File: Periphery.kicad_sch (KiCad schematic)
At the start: 22 parts, among them SW1 Mitsumi R-667996, SW2 Mitsumi R-667996, U2 SN74LV595A, U3 THVD1420DRLR, U4 RS31340B, U5 SN74LV595A, U6 TS5A3159DCK

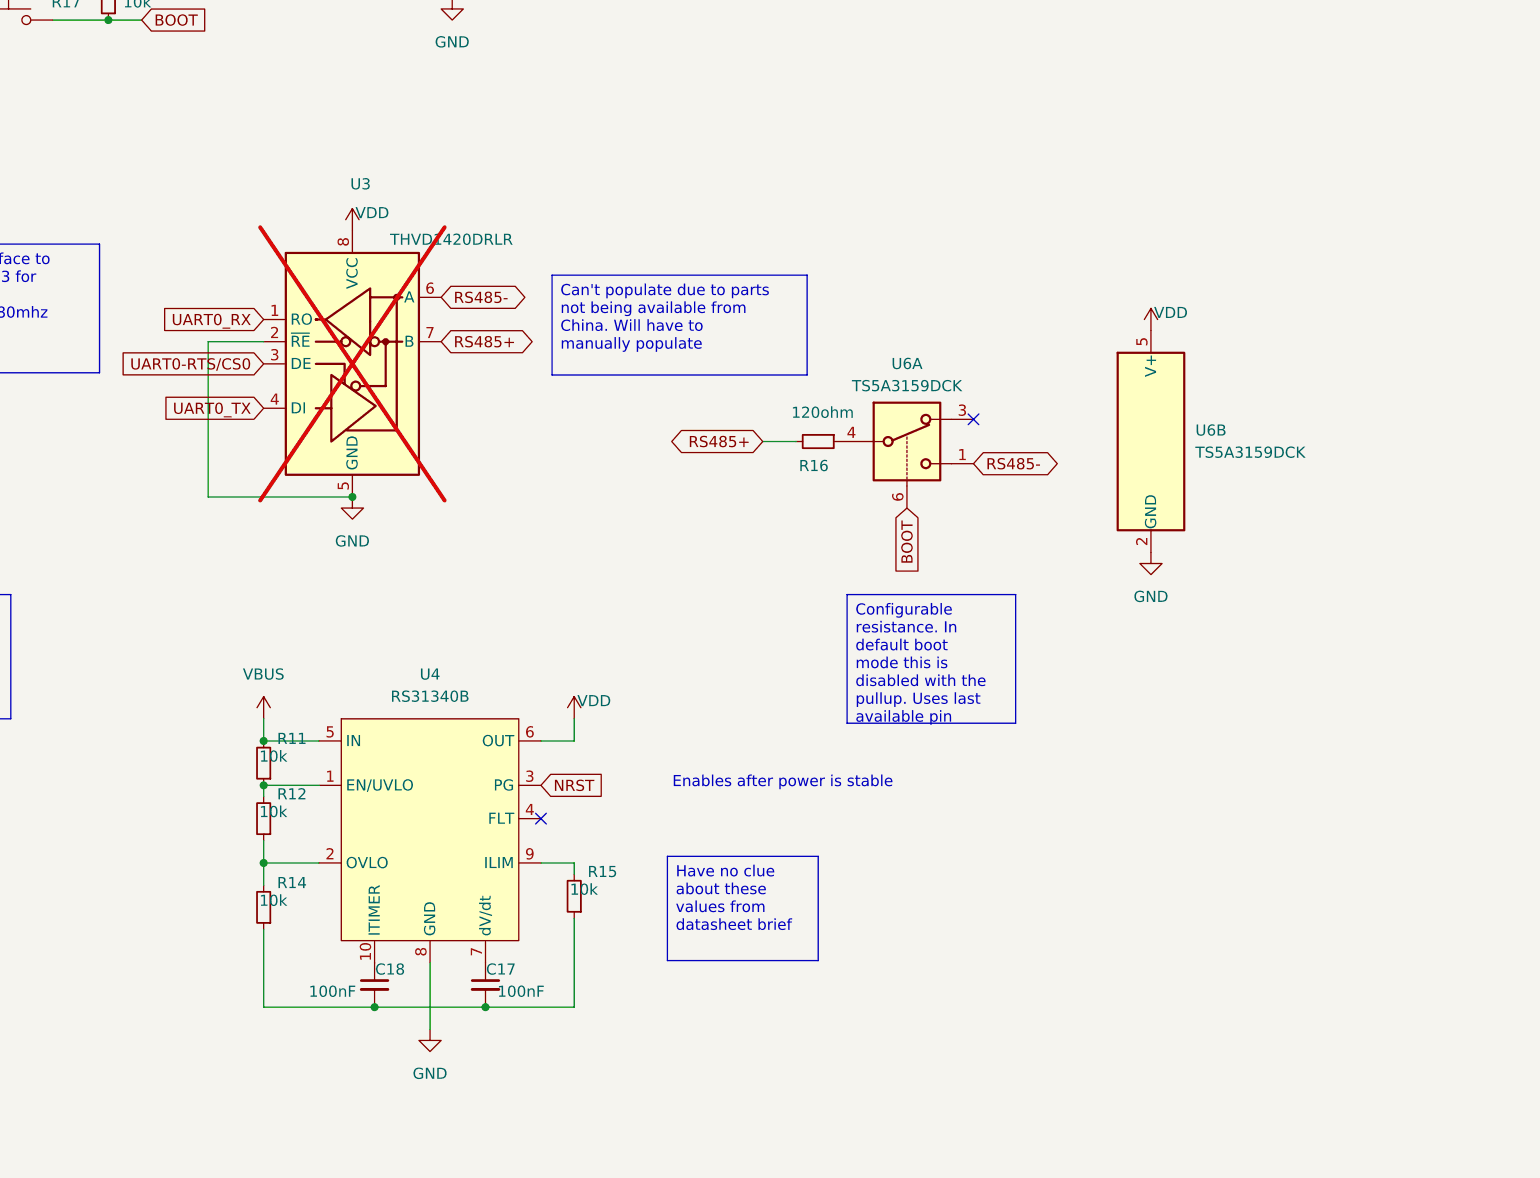
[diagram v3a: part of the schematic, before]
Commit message: Got proper values and replacement eFuse
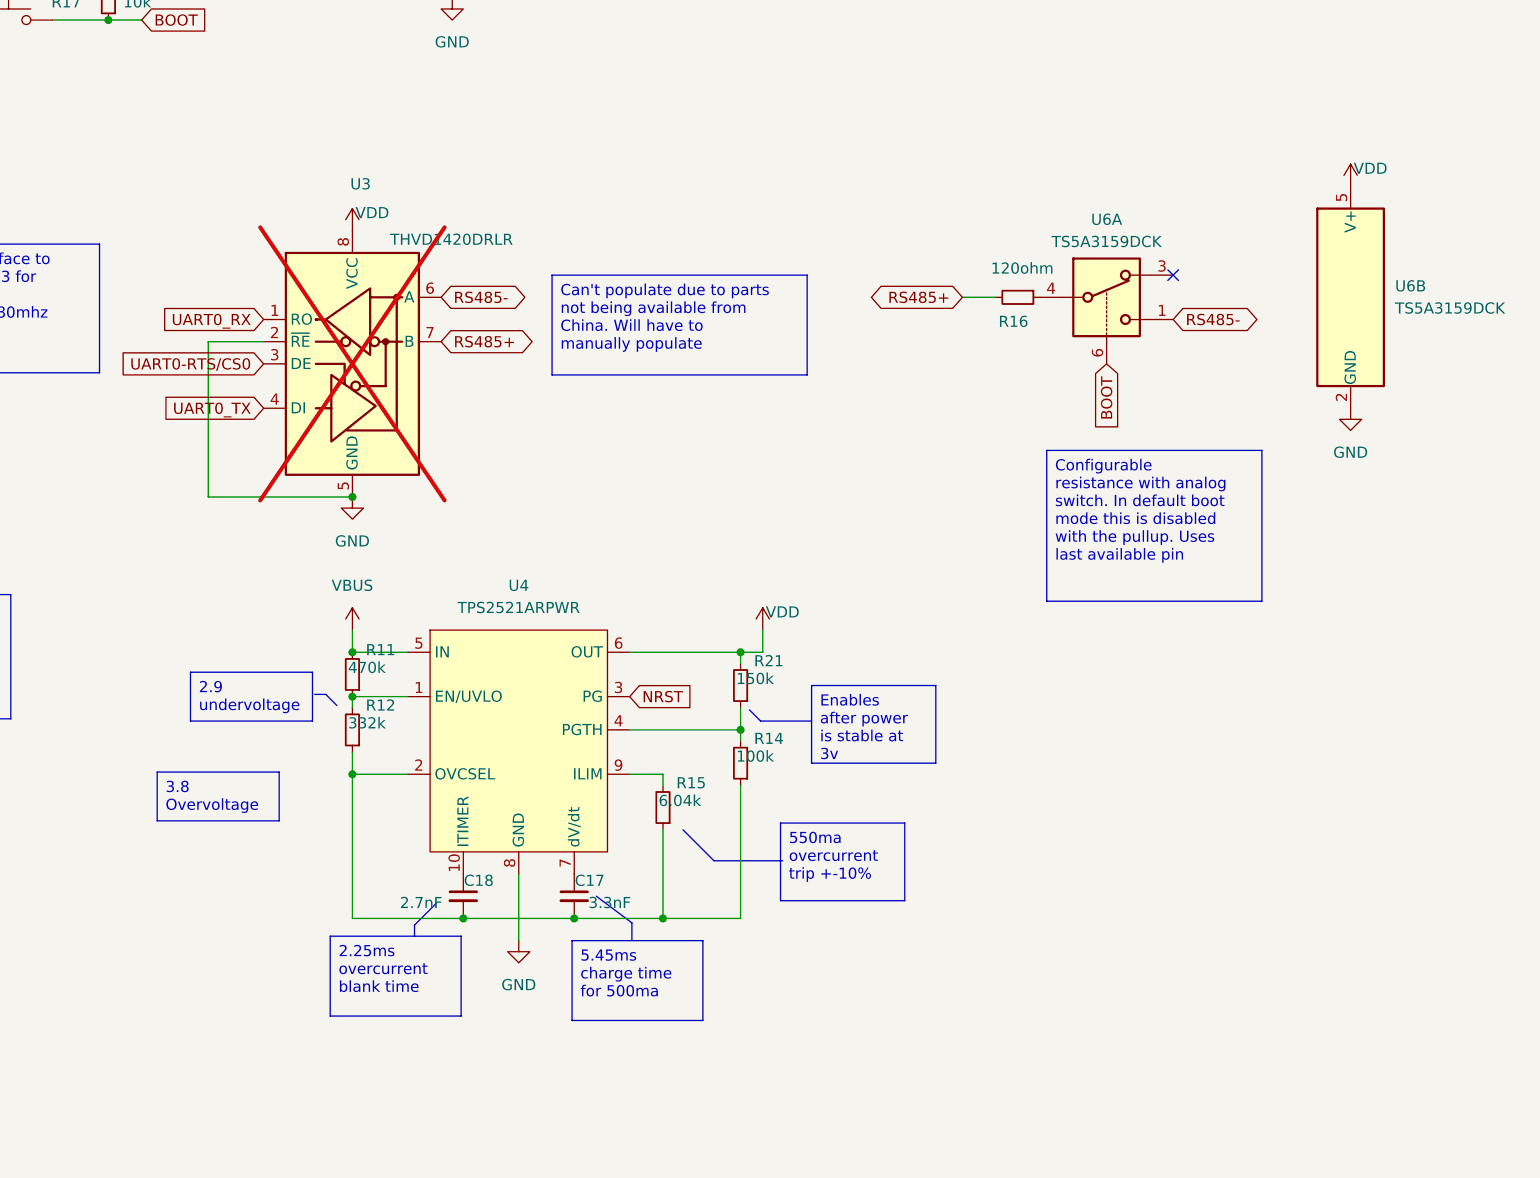
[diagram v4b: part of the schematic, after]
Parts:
- added R21: 150k, Resistor_SMD:R_0402_1005Metric, symbol Device:R_Small
- C17: value 100nF -> 3.3nF
- C18: value 100nF -> 2.7nF
- R11: value 10k -> 470k
- R12: value 10k -> 332k
- R14: value 10k -> 100k
- R15: value 10k -> 6.04k
- U4: value RS31340B -> TPS2521ARPWR; symbol custom_Power_Management:RS31340 -> custom_Power_Management:TPS2521xx
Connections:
- net VDD: now also R21.2
- net at C17.2, C18.2, R14.1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: now also R12.1, U4.2 (OVCSEL)
- net at U4.4 (PGTH): now also R14.2, R21.1
- no-connect marks 3 -> 2
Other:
- note removed: "Enables after power is stable"
- moved on the sheet: C17, C18, R11, R12, R15, R16, U4, U6A, U6B

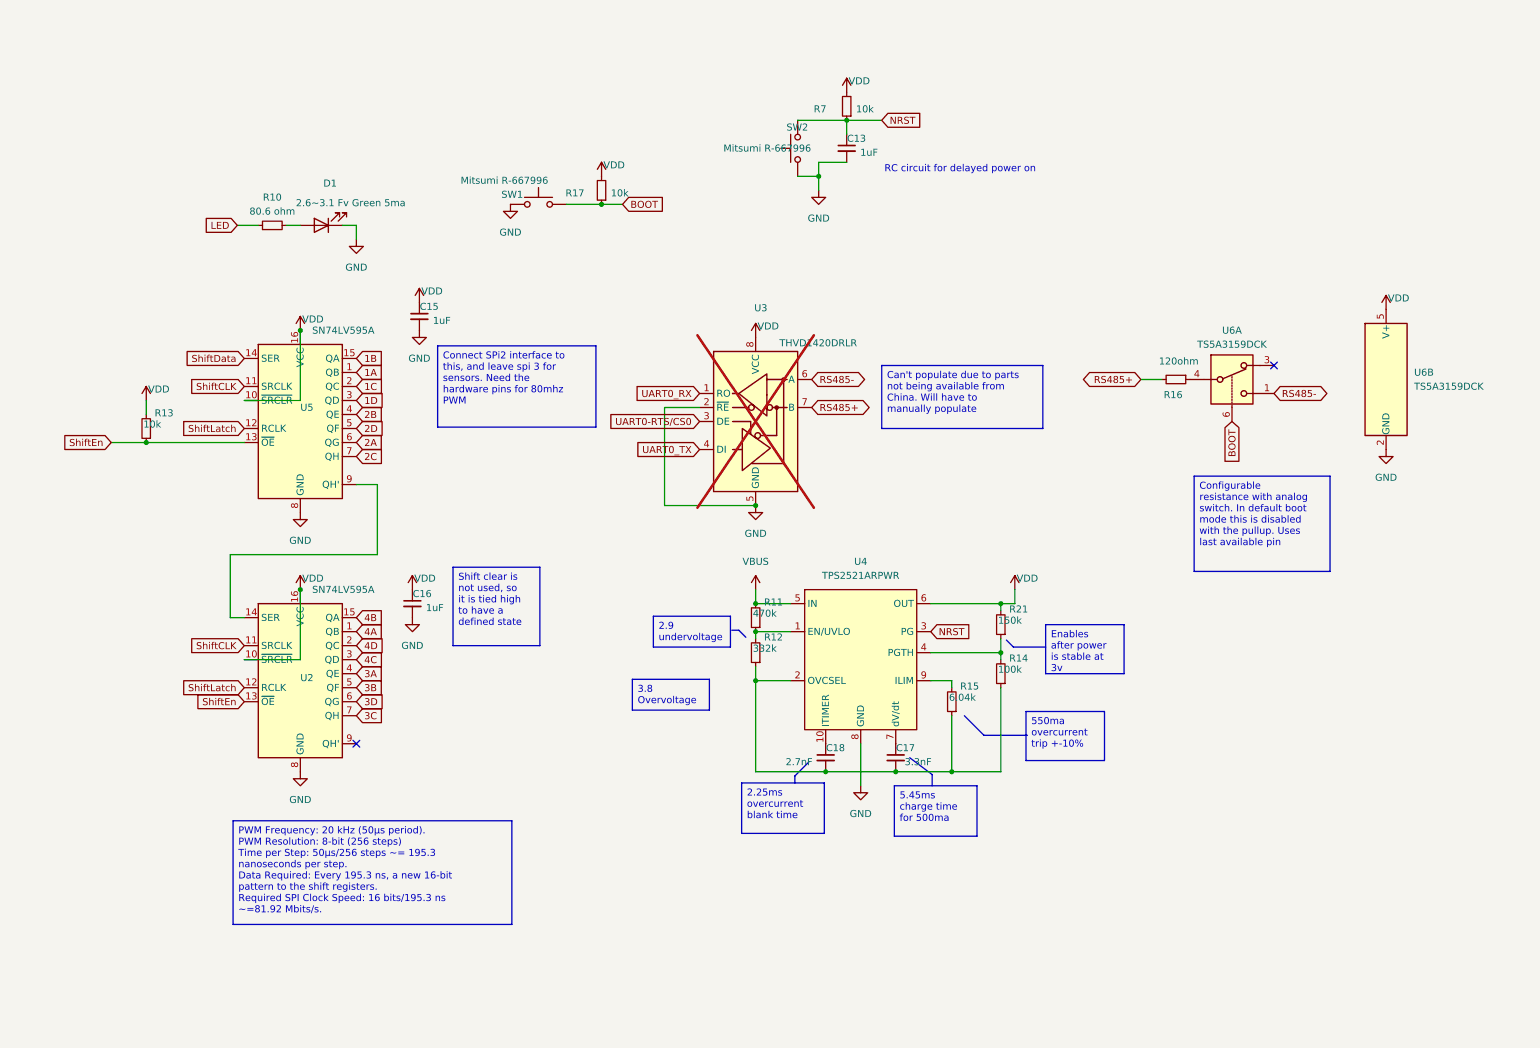
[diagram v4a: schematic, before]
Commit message: Reorganized and made schematic clearer
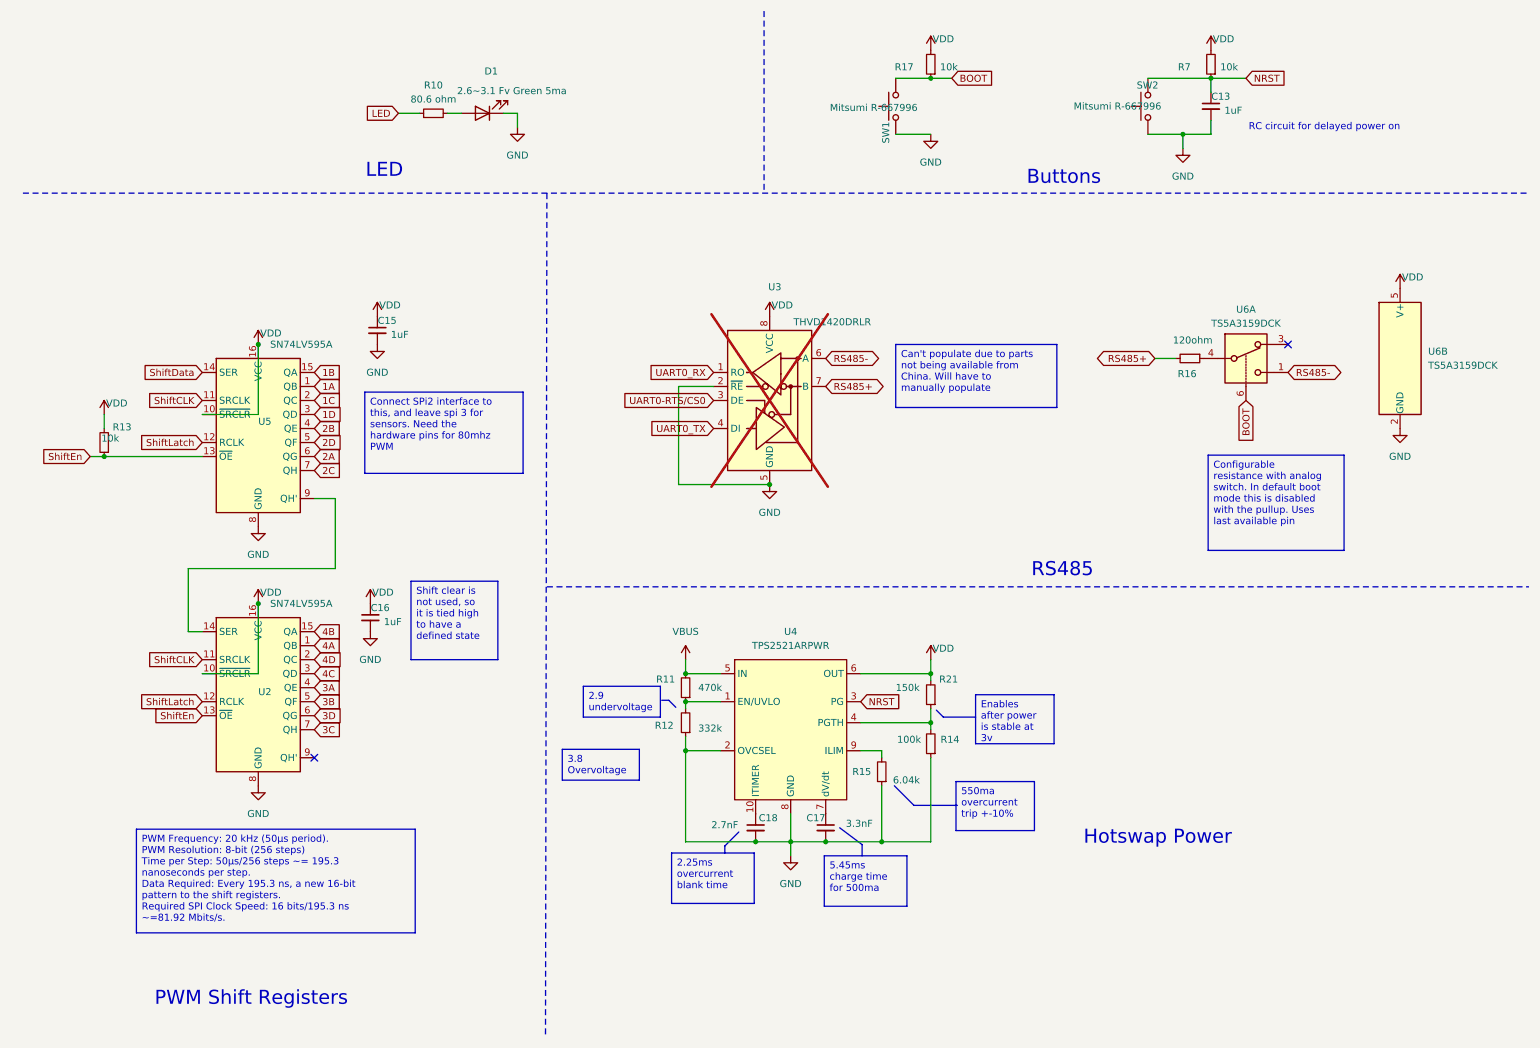
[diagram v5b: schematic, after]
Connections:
- net GND: now also C17.2, C18.2, R12.1, R14.1, R15.1, U2.17 (GND), U4.2 (OVCSEL), U5.17 (GND)
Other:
- note added: "Buttons"
- note added: "Hotswap Power"
- note added: "LED"
- note added: "PWM Shift Registers"
- note added: "RS485"
- moved on the sheet: C13, C15, C16, C17, C18, D1, R10, R11, R12, R13, R14, R15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

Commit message: Corrected footprint, started reconnect nets PCB
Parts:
- U4: footprint custom_Power_QFN:QFN-10-1EP_2x2mm_P0.5mm -> custom_Power_QFN:QFN-10_10VQFN_2x2mm_P0.5mm
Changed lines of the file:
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@@
 			)
 		)
-		(property "Footprint" "custom_Power_QFN:QFN-10-1EP_2x2mm_P0.5mm"
+		(property "Footprint" "custom_Power_QFN:QFN-10_10VQFN_2x2mm_P0.5mm"
 			(at 151.13 142.24 0)
 			(effects

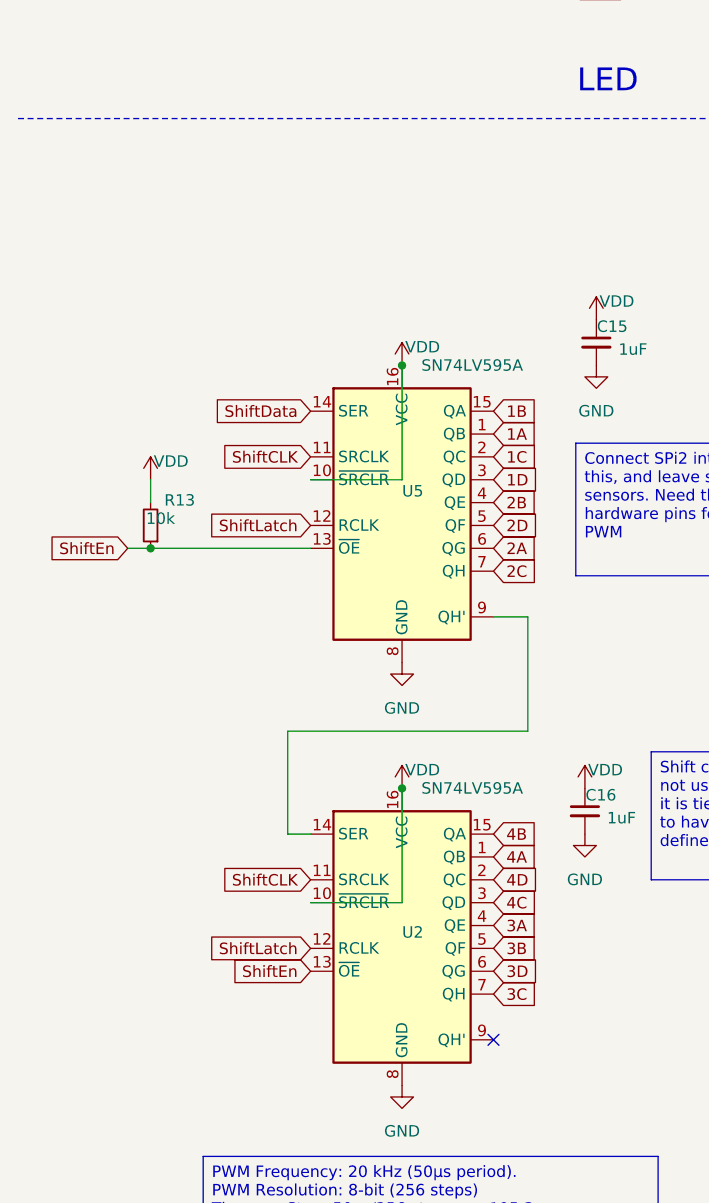
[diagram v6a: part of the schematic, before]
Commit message: Finished Reroute of ESP32-s3 hub
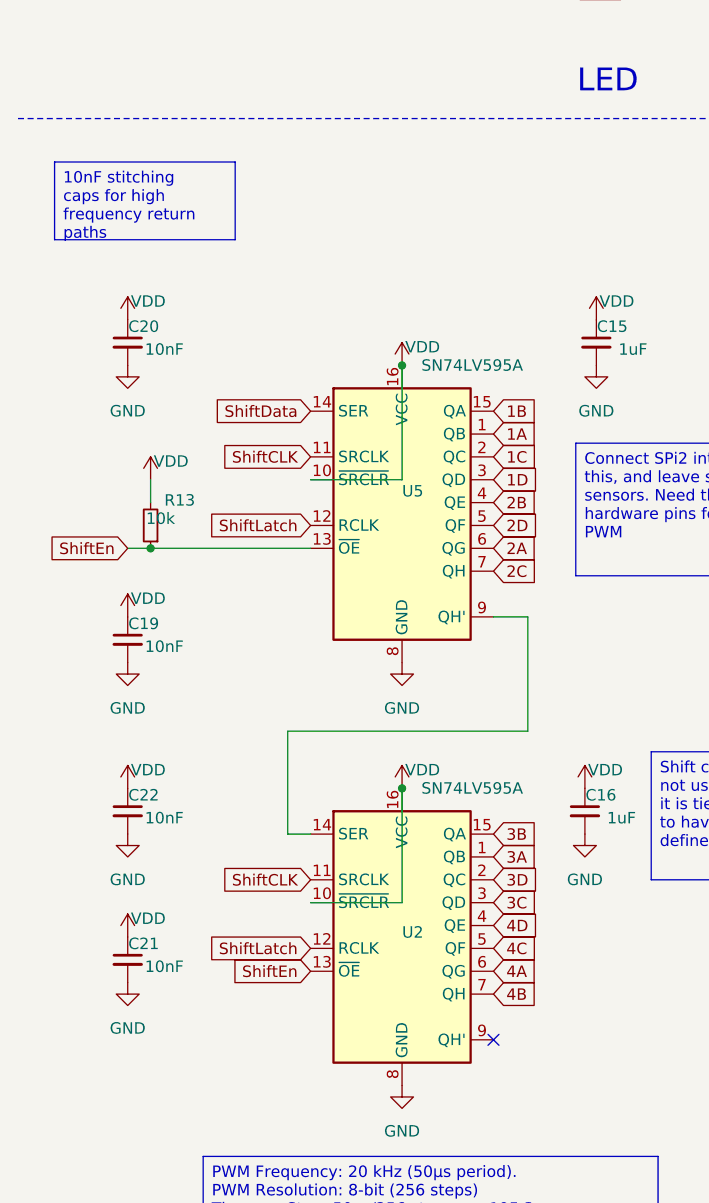
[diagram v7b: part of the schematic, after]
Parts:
- added C19, C20, C21, C22: 10nF, Capacitor_SMD:C_0402_1005Metric, symbol Device:C_Small
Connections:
- net 3A: now also U2.1 (QB); no longer U2.4 (QE)
- net 3B: now also U2.15 (QA); no longer U2.5 (QF)
- net 3C: now also U2.3 (QD); no longer U2.7 (QH)
- net 3D: now also U2.2 (QC); no longer U2.6 (QG)
- net 4A: now also U2.6 (QG); no longer U2.1 (QB)
- net 4B: now also U2.7 (QH); no longer U2.15 (QA)
- net 4C: now also U2.5 (QF); no longer U2.3 (QD)
- net 4D: now also U2.4 (QE); no longer U2.2 (QC)
- net GND: now also C19.2, C20.2, C21.2, C22.2
- net VDD: now also C19.1, C20.1, C21.1, C22.1

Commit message: Improve schematic consistency
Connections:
- net 1A renamed PWM-1A
- net 1B renamed PWM-1B
- net 1C renamed PWM-1C
- net 1D renamed PWM-1D
- net 2A renamed PWM-2A
- net 2B renamed PWM-2B
- net 2C renamed PWM-2C
- net 2D renamed PWM-2D
- net 3A renamed PWM-3A
- net 3B renamed PWM-3B
- net 3C renamed PWM-3C
- net 3D renamed PWM-3D
- net 4A renamed PWM-4A
- net 4B renamed PWM-4B
- net 4C renamed PWM-4C
- net 4D renamed PWM-4D
- net UART0-RTS/CS0 renamed UART0-RTS
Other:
- moved on the sheet: C15, C16, C19, C20, C21, C22, D1, R13
